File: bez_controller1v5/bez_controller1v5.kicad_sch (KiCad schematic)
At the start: 76 parts, among them J1 Conn_01x03_Male, J10 Conn_01x07_Socket, J11 Conn_01x03_Male, J12 Conn_01x03_Male, J13 USB_B_Mini, J14 JTAG Conn_01x06_Male, J2 Conn_01x03_Male, J3 Conn_01x03_Male, J4 Screw_Terminal_01x02, J5 Conn_01x03_Male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

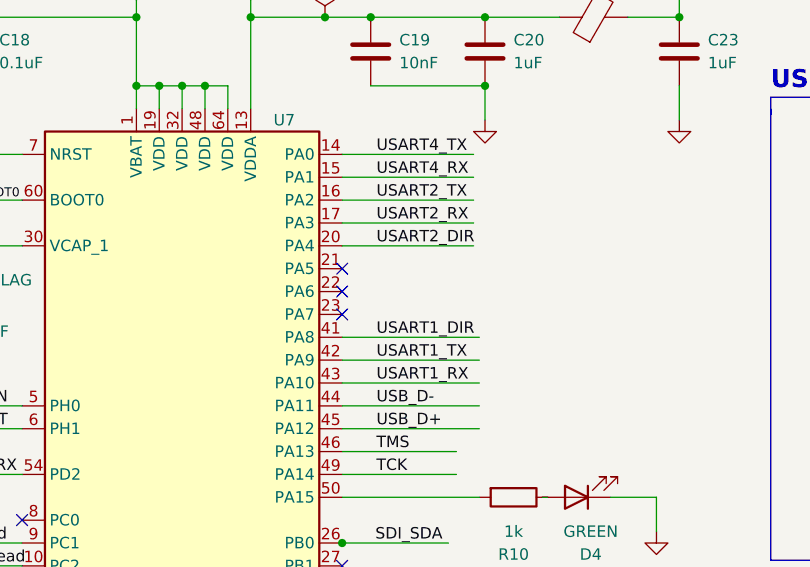
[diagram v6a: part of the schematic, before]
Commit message: connected SPI
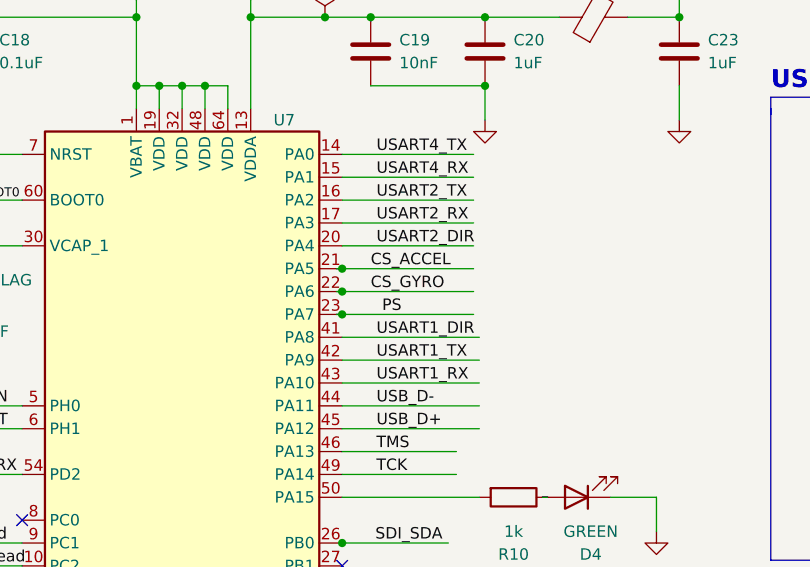
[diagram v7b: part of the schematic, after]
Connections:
- net CS_ACCEL: now also U7.21 (PA5)
- net CS_GYRO: now also U7.22 (PA6)
- net PS: now also U7.23 (PA7)
- no-connect marks 21 -> 18
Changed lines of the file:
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@@
   (junction (at 22.225 139.7) (diameter 0) (color 0 0 0 0)
   )
+  (junction (at 140.335 116.84) (diameter 0) (color 0 0 0 0)
+  )
   (junction (at 19.685 27.94) (diameter 0) (color 0 0 0 0)
   )
@@
   (junction (at 138.43 88.9) (diameter 0) (color 0 0 0 0)
   )
+  (junction (at 140.335 119.38) (diameter 0) (color 0 0 0 0)
+  )
   (junction (at 267.97 -102.235) (diameter 0) (color 0 0 0 0)
   )
@@
   )
   (junction (at 47.625 29.21) (diameter 0) (color 0 0 0 0)
+  )
+  (junction (at 140.335 121.92) (diameter 0) (color 0 0 0 0)
   )
   (junction (at 22.225 153.67) (diameter 0) (color 0 0 0 0)
@@
   (no_connect (at 266.7 130.175))
   (no_connect (at 140.335 175.26))
-  (no_connect (at 140.335 116.84))
   (no_connect (at 104.775 167.64))
   (no_connect (at 140.335 160.02))
@@
   (no_connect (at 140.335 149.86))
   (no_connect (at 276.86 135.255))
-  (no_connect (at 140.335 121.92))
   (no_connect (at 104.775 154.94))
   (no_connect (at 235.204 50.038))
@@
   (no_connect (at 235.204 44.958))
   (no_connect (at 104.775 144.78))
-  (no_connect (at 140.335 119.38))
   (wire (pts (xy 76.2 27.305) (xy 76.2 29.21))
     (stroke (width 0) (type default))
@@
     (stroke (width 0) (type default))
   )
+  (wire (pts (xy 140.335 119.38) (xy 154.94 119.38))
+    (stroke (width 0) (type default))
+  )
   (wire (pts (xy 209.55 -93.98) (xy 220.98 -93.98))
     (stroke (width 0) (type default))
@@
     (stroke (width 0) (type default))
   )
+  (wire (pts (xy 140.335 121.92) (xy 154.94 121.92))
+    (stroke (width 0) (type default))
+  )
   (polyline (pts (xy 187.96 97.79) (xy 187.96 99.695))
     (stroke (width 0) (type default))
@@
     (stroke (width 0) (type default))
   )
+  (wire (pts (xy 139.7 116.84) (xy 140.335 116.84))
+    (stroke (width 0) (type default))
+  )
   (wire (pts (xy 234.95 -102.235) (xy 267.97 -102.235))
     (stroke (width 0) (type default))
@@
     (stroke (width 0) (type default))
   )
+  (wire (pts (xy 139.7 119.38) (xy 140.335 119.38))
+    (stroke (width 0) (type default))
+  )
   (wire (pts (xy 234.95 -109.855) (xy 234.95 -102.235))
     (stroke (width 0) (type default))
@@
     (stroke (width 0) (type default))
   )
+  (wire (pts (xy 139.7 121.92) (xy 140.335 121.92))
+    (stroke (width 0) (type default))
+  )
   (wire (pts (xy 160.782 53.848) (xy 160.782 51.308))
     (stroke (width 0) (type default))
@@
   )
   (wire (pts (xy 234.95 -102.235) (xy 234.95 -93.98))
+    (stroke (width 0) (type default))
+  )
+  (wire (pts (xy 140.335 116.84) (xy 154.94 116.84))
     (stroke (width 0) (type default))
   )
@@
     (effects (font (size 1.27 1.27)) (justify left bottom))
   )
+  (label "CS_ACCEL" (at 143.51 116.84 0) (fields_autoplaced)
+    (effects (font (size 1.27 1.27)) (justify left bottom))
+  )
   (label "USART5_RX" (at 125.73 -36.83 180) (fields_autoplaced)
     (effects (font (size 1.27 1.27)) (justify right bottom))
@@
     (effects (font (size 1.27 1.27)) (justify left bottom))
   )
+  (label "PS" (at 144.78 121.92 0) (fields_autoplaced)
+    (effects (font (size 1.27 1.27)) (justify left bottom))
+  )
   (label "USART2_TX" (at 144.145 109.22 0) (fields_autoplaced)
     (effects (font (size 1.27 1.27)) (justify left bottom))
@@
     (effects (font (size 1.27 1.27)) (justify left bottom))
   )
+  (label "CS_GYRO" (at 143.51 119.38 0) (fields_autoplaced)
+    (effects (font (size 1.27 1.27)) (justify left bottom))
+  )

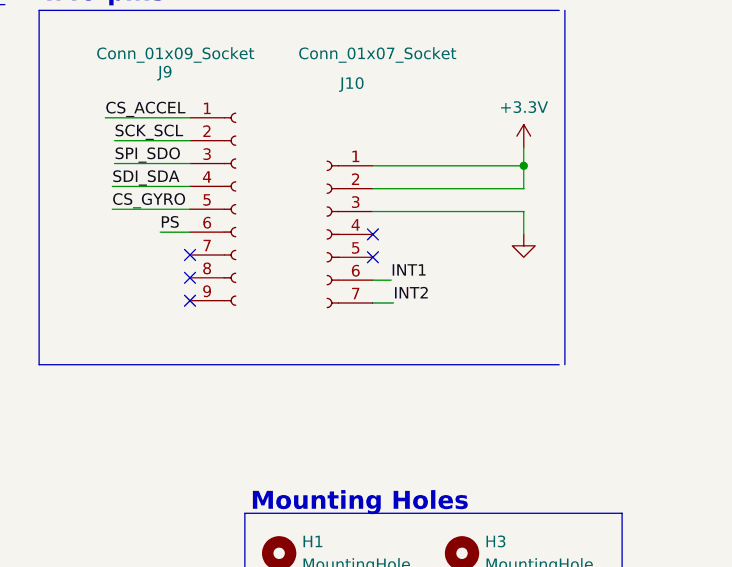
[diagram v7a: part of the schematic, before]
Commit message: remove warnings, clean up labels, redo some wiring
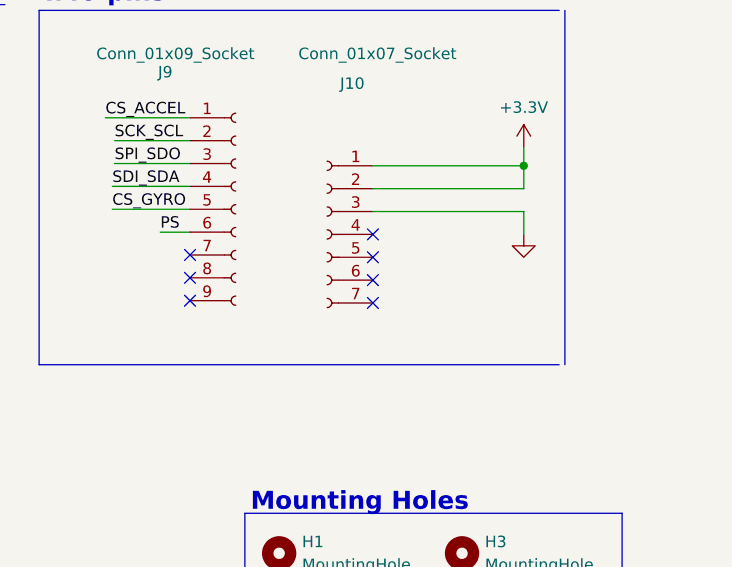
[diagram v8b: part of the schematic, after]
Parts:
- J13: footprint Connector_USB:USB_Micro-B_Molex-105017-0001 -> USB-Library:USB_MINI
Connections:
- net INT1: no longer names the net of J10.6 (Pin_6)
- net INT2: no longer names the net of J10.7 (Pin_7)
- no-connect marks 18 -> 20
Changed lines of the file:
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@@
   (no_connect (at 255.524 42.672))
   (no_connect (at 140.335 170.18))
+  (no_connect (at 255.524 50.292))
   (no_connect (at 140.335 167.64))
   (no_connect (at 266.7 130.175))
   (no_connect (at 140.335 175.26))
+  (no_connect (at 255.524 47.752))
   (no_connect (at 104.775 167.64))
   (no_connect (at 140.335 160.02))
@@
     (stroke (width 0) (type default))
   )
-  (wire (pts (xy 255.524 47.752) (xy 257.556 47.752))
-    (stroke (width 0) (type default))
-  )
   (polyline (pts (xy 283.21 90.805) (xy 283.21 73.66))
     (stroke (width 0) (type default))
@@
     (stroke (width 0) (type default))
   )
-  (wire (pts (xy 255.524 50.292) (xy 257.81 50.292))
-    (stroke (width 0) (type default))
-  )
   (wire (pts (xy 257.81 -60.96) (xy 260.985 -60.96))
     (stroke (width 0) (type default))
@@
     (effects (font (size 1.27 1.27)) (justify left bottom))
   )
-  (label "INT2" (at 257.81 50.292 0) (fields_autoplaced)
-    (effects (font (size 1.27 1.27)) (justify left bottom))
-  )
   (label "GPIO1" (at 95.25 182.88 0) (fields_autoplaced)
     (effects (font (size 1.27 1.27)) (justify left bottom))
@@
     (effects (font (size 1.27 1.27)) (justify left bottom))
   )
-  (label "INT1" (at 257.556 47.752 0) (fields_autoplaced)
-    (effects (font (size 1.27 1.27)) (justify left bottom))
-  )
   (label "V_shunt_read" (at 135.255 57.785 0) (fields_autoplaced)
     (effects (font (size 1.27 1.27)) (justify left bottom))
@@
       (effects (font (size 1.27 1.27)) (justify right))
     )
-    (property "Footprint" "Connector_USB:USB_Micro-B_Molex-105017-0001" (at 270.51 126.365 0)
+    (property "Footprint" "USB-Library:USB_MINI" (at 270.51 126.365 0)
       (effects (font (size 1.27 1.27)) hide)
     )
